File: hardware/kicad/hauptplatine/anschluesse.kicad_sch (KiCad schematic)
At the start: 9 parts, among them J701 DS18B20 Nr. 1, J702 DS18B20 Nr. 2, J703 BME280, J704 Erweiterung

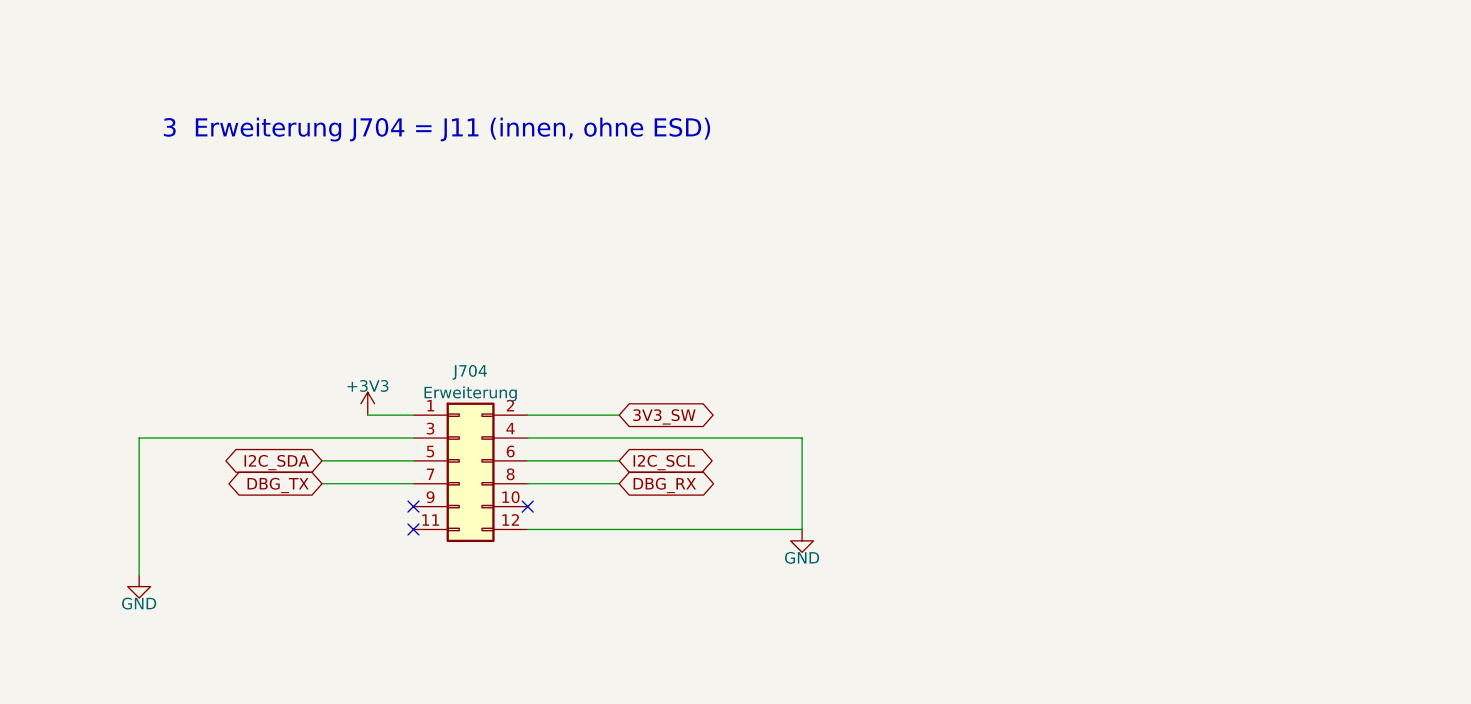
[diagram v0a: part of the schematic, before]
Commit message: HW-09: BLE-Modul RN4871 an USART6 statt USB-Daten, USB-C nur Laden
Warum: Service-Zugang ohne Öffnen des Gehäuses (Lastenheft F7); Vorschlagspaket
„USB → BLE RN4871“ vom 18.10.2026 geprüft und eingearbeitet (Pinwahl USART6
PA11/PA12 bestätigt, Modul übernommen; Versorgung, Reset und USB-Laden anders).

Was:
- Blatt MCU: U303 RN4871-I/RM130 (C633942) an USART6 über R310/R311 1 kΩ;
  Lastschalter Q301 AO3401A an PB13 (low = ein, R309 100k), C314/C315 an VBAT,
  R312 10k (P2_0) an BLE_VCC, C316 an RST_N, JP301 „BLE dauernd“, #FLG302.
- USB-C J301 nur Laden: D+/D− offen, U302 und R307/R308 entfernt (SCH26-10
  gegenstandslos). J704 Pin 9–11 = BLE_RXD/BLE_TXD/BLE_MODE.
- Symbol Bienen:RN4871 (DS50002489D Tab. 1-2), Footprint Bienen:Microchip_RN4871
  mit Sperrzonen (Antenne *.Cu, Testpunkte F.Cu) nach Fig. 4-7/4-8 [A].
- netz_tests.py: ble() mit Gegenprobe, J704/J11, USB ohne Daten;
  pin_footprint.py: RN4871 [V], AO3401A.
- Dokumente: mcu-funk.md 1.3/1.6, Lastenheft K5/K6/F9/M5/M8, anschluesse.md,
  versorgung.md, energiebilanz.py (2a BLE-Sitzung), Pflichtenheft/Fiverr,
  KiCad-README, Entscheidungsregister HW-09, Befundregister HW26-20, CHANGELOG,
  Bericht docs/testberichte/2026-10-18-hw09-ble-rn4871.md.

Offen (Philipp): USB-C-Buchse als Ladebuchse behalten (umgesetzt) oder entfernen.

Tests (T0/T3, KiCad 10.0.7 Windows): pruefen.sh reproduzierbar, ERC 0,
Netzprüfung 220/220, Pin/Footprint 179/0; energiebilanz.py, i2c_leitung.py,
netz_vergleich.py --selbsttest ok. Keine Messung, keine BLE-Firmware;
alle_tests_linux.sh nicht lokal gelaufen (CI).

Co-Authored-By: Claude Fable 5.1 <noreply@anthropic.com>
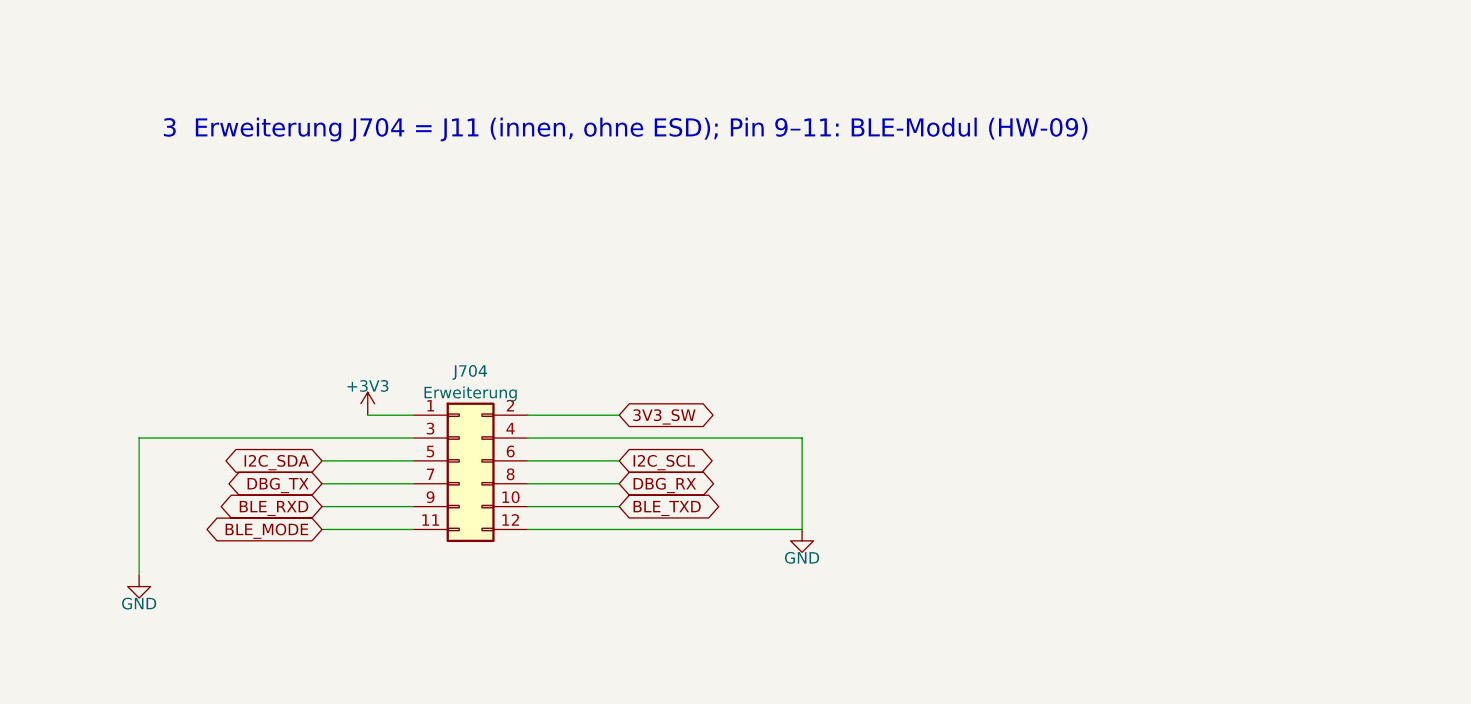
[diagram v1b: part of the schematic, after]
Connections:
- net BLE_TXD: now reaches J704.10 (Pin_10)
- net BLE_MODE: now reaches J704.11 (Pin_11)
- net BLE_RXD: now reaches J704.9 (Pin_9)
- no-connect marks 7 -> 4
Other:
- note added: "3 Erweiterung J704 = J11 (innen, ohne ESD); Pin 9–11: BLE-Modul (HW-09)"
- note removed: "3 Erweiterung J704 = J11 (innen, ohne ESD)"
